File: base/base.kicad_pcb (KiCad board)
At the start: 2 copper layers, 100 x 100 mm, 20 parts, among them J1 FTDI, J2 Barrel_Jack, J3 CONN_01X40, SW1 SW_Push, U1 Z80CPU, U2 27C256, U3 7404, U4 55257, U5 7432, U6 16550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

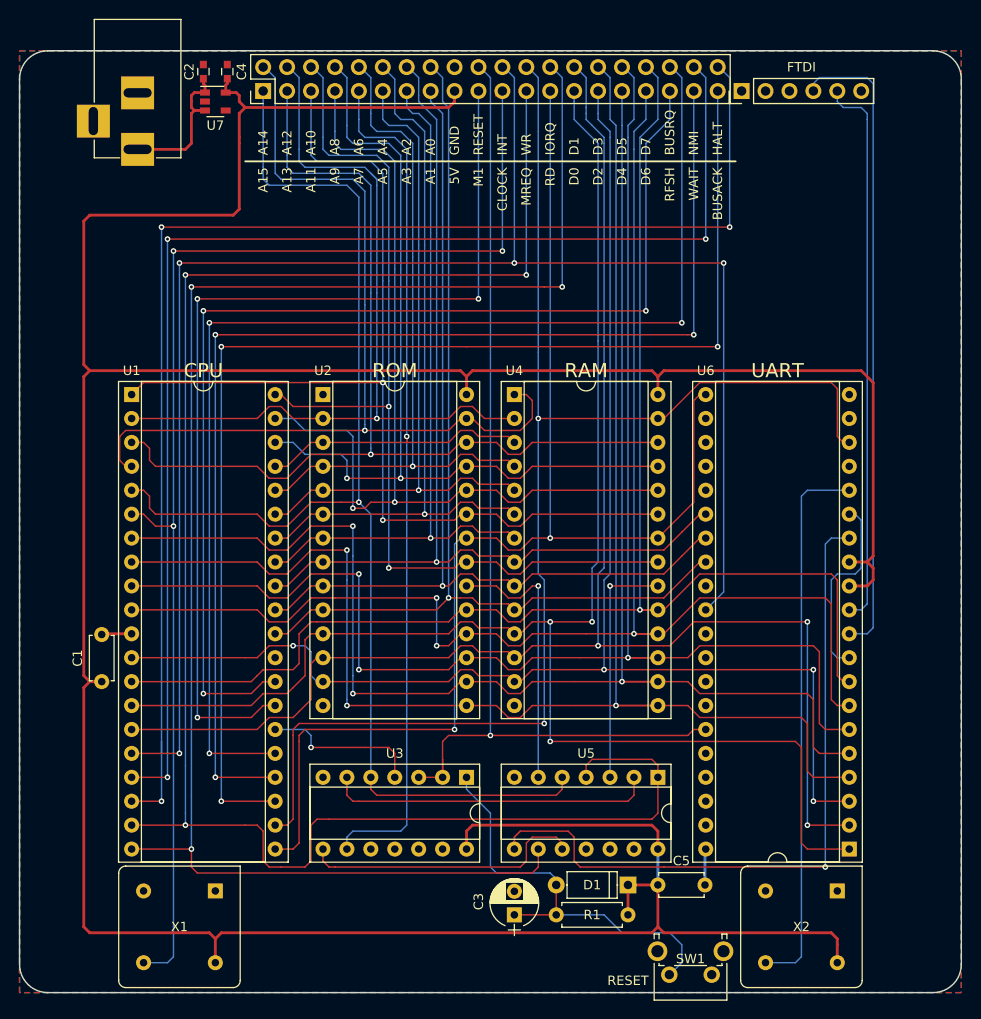
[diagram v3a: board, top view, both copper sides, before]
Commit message: Readded mounting holes
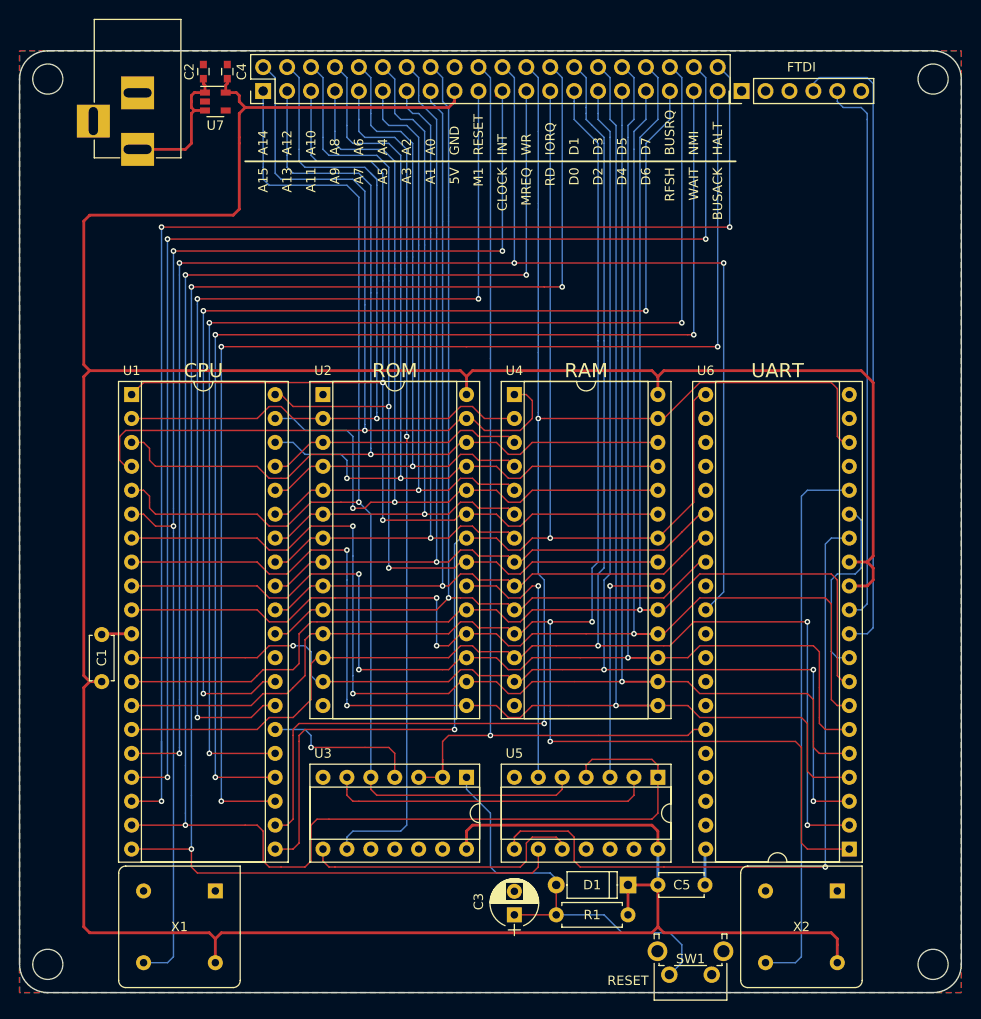
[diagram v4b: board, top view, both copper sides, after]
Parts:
- added REF**: MountingHole_3.2mm_M3, Mounting_Holes:MountingHole_3.2mm_M3, F.Cu at (151.1, 157.0)
- added REF**: MountingHole_3.2mm_M3, Mounting_Holes:MountingHole_3.2mm_M3, F.Cu at (57.1, 157.0)
- added REF**: MountingHole_3.2mm_M3, Mounting_Holes:MountingHole_3.2mm_M3, F.Cu at (57.1, 63.0)
- added REF**: MountingHole_3.2mm_M3, Mounting_Holes:MountingHole_3.2mm_M3, F.Cu at (151.1, 63.0)
- added REF***: OSHW-Symbol_6.7x6mm_SilkScreen, Symbols:OSHW-Symbol_6.7x6mm_SilkScreen, B.Cu at (104.1, 73.0)
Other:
- board text added: "6-20V"

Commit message: Redid power trace
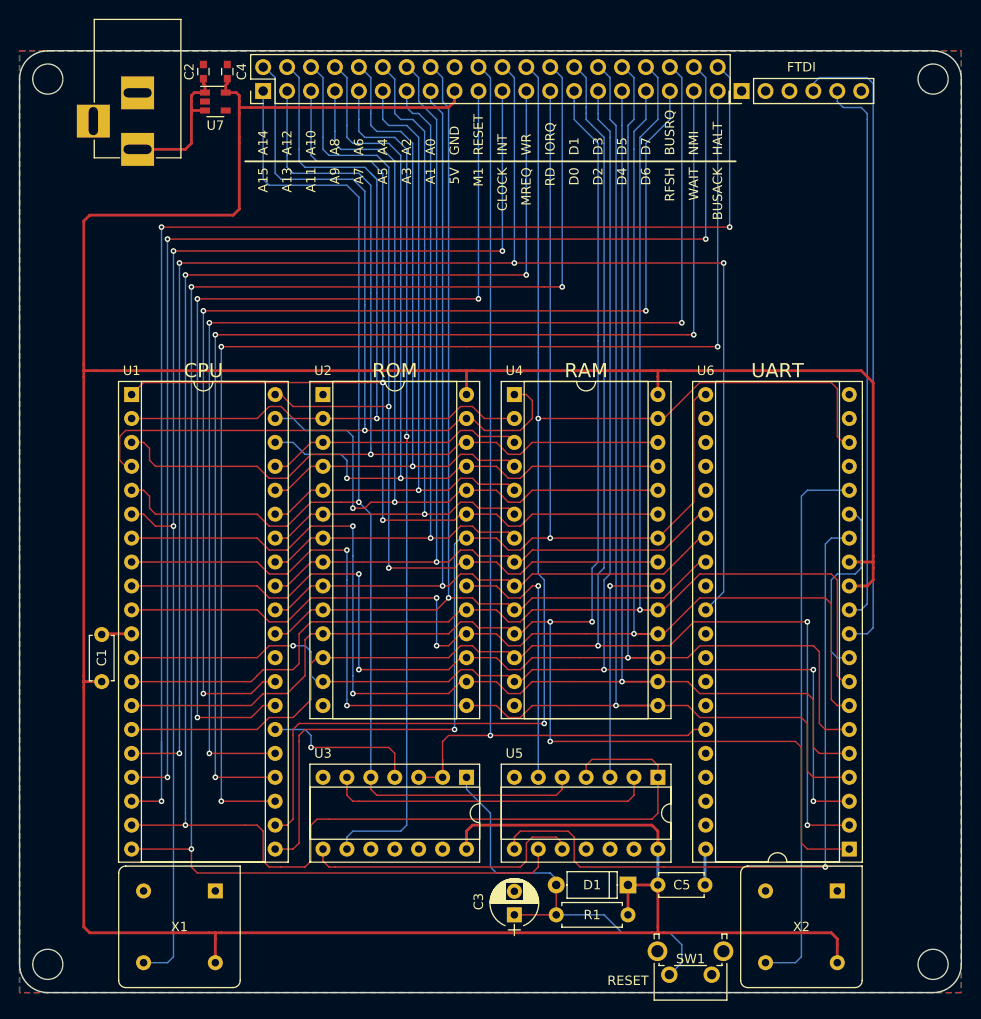
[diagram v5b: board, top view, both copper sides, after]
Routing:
- net +5V: track 374.9 -> 375.8 mm

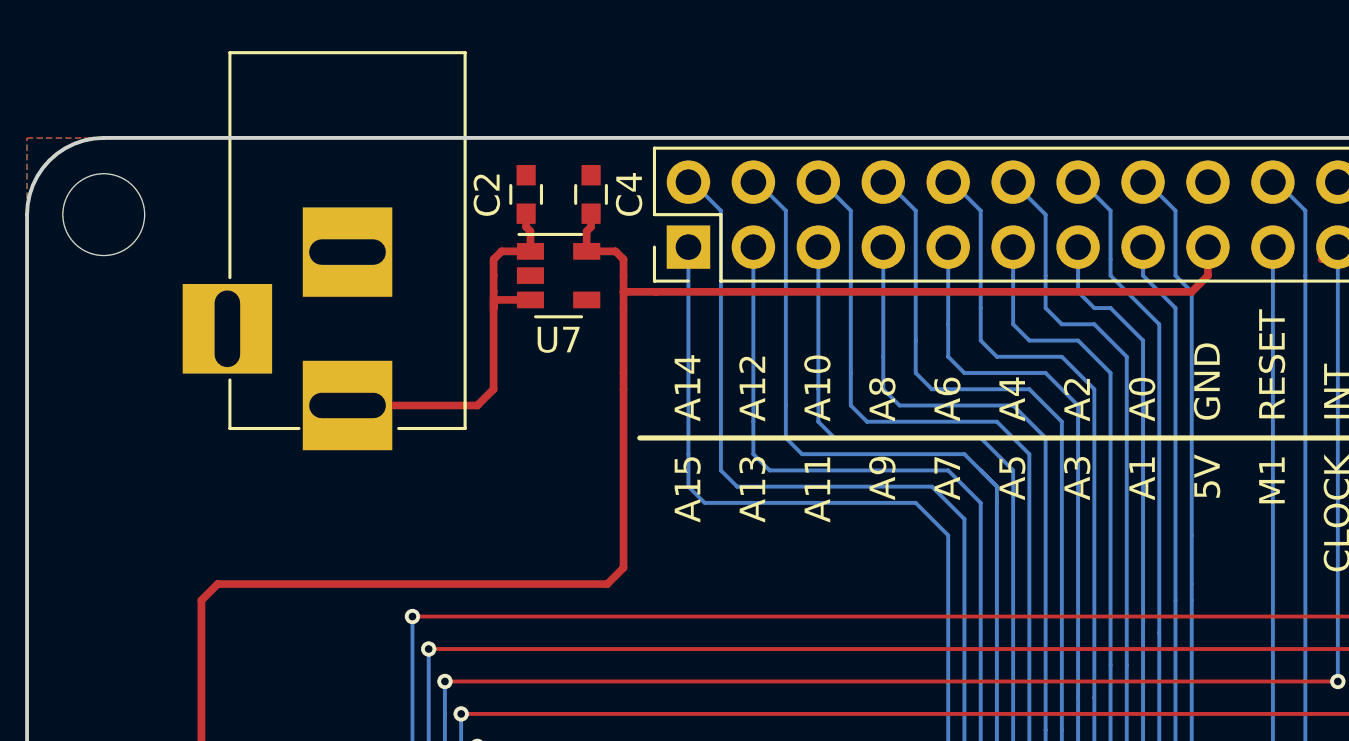
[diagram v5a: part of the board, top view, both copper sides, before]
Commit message: Increased size of voltage regulator
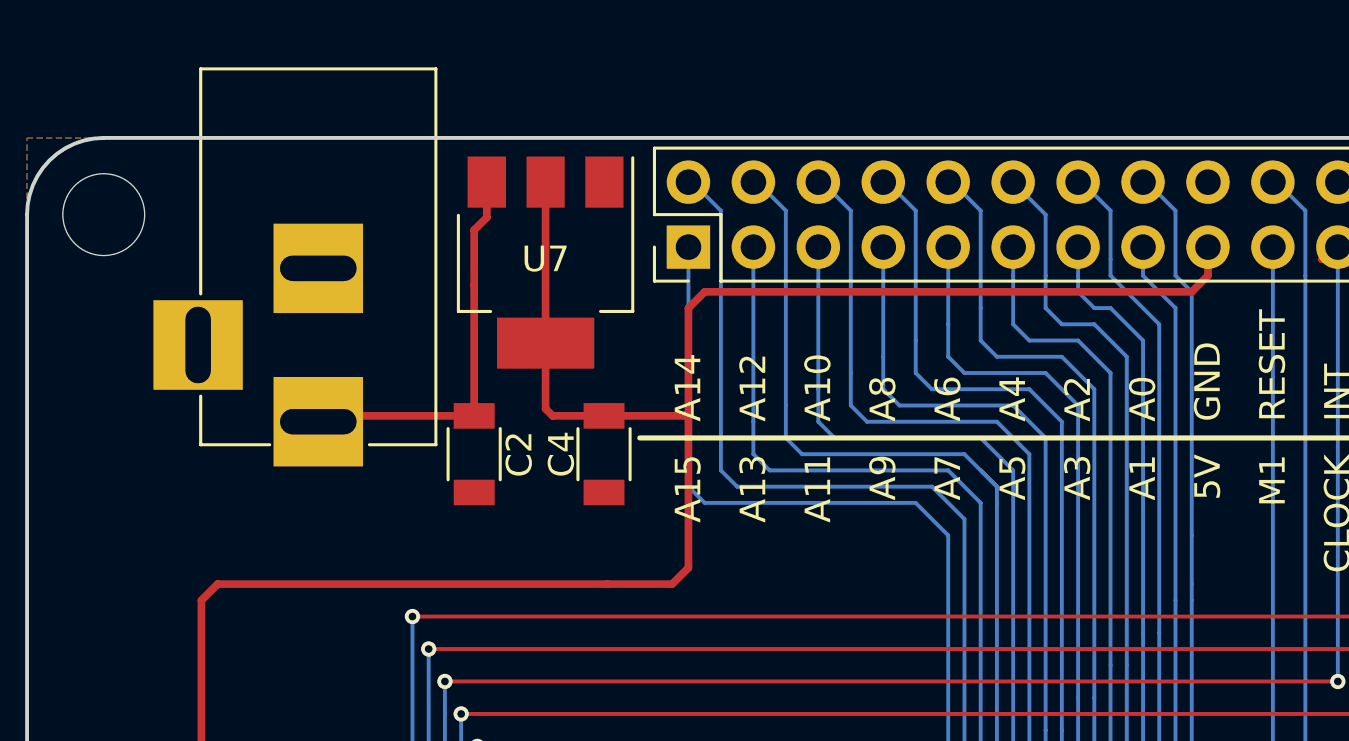
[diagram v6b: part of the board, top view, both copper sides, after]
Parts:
- C1: value .1 uF -> 1 uF
- C2, C4: value 1 uF -> 10 uF; footprint Capacitors_SMD:C_0603 -> Capacitors_SMD:C_1206
- C5: value .1 uF -> C_Small
- U7: value MIC5205-5.0 -> AP1117-50; footprint TO_SOT_Packages_SMD:SOT-23-5 -> TO_SOT_Packages_SMD:SOT-223-3Lead_TabPin2
- moved C2 10.4 mm to (71.6, 72.4), turned to 270 degrees
- moved C4 10.2 mm to (76.7, 72.4), turned to 270 degrees
- moved J2 1.31 mm to (65.5, 71.1)
- moved U7 0.72 mm to (74.4, 64.9), turned to 270 degrees
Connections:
- U7 pad 1: Net-(C2-Pad1) -> GND
- U7 pad 2: GND -> +5V
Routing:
- net +5V: track 375.8 -> 385.9 mm
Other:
- board text added: "7-15V"
- board text removed: "6-20V"

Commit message: Moved FTDI port
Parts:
- moved J1 2.54 mm to (133.3, 64.3)
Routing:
- net TX: track 68.3 -> 65.7 mm
- net RX: track 59.1 -> 56.9 mm
- net Net-(J1-Pad3): track 0.00 -> 0.79 mm
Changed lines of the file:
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@@
     (thickness 1.6)
     (drawings 57)
-    (tracks 1103)
+    (tracks 1102)
     (zones 0)
     (modules 25)
@@
   )
   (module Pin_Headers:Pin_Header_Straight_1x06_Pitch2.54mm (layer F.Cu)
-    (at 130.81 64.29 90)
+    (at 133.35 64.29 90)
     (descr "Through hole straight pin header, 1x06, 2.54mm pitch, single row")
     (tags "Through hole pin header THT 1x06 2.54mm single row")
@@
   (segment (start 104.14 92.71) (end 104.14 132.715) (width 0.152) (layer B.Cu) (net 55))
   (via (at 104.14 132.715) (size 0.6) (drill 0.3) (layers F.Cu B.Cu) (net 55))
+  (segment (start 144.145 66.675) (end 143.51 66.04) (width 0.152) (layer B.Cu) (net 58))
+  (segment (start 143.51 66.04) (end 143.51 64.29) (width 0.152) (layer B.Cu) (net 58) (status 800000))
   (segment (start 144.145 67.31) (end 144.145 118.745) (width 0.152) (layer B.Cu) (net 58))
-  (segment (start 140.97 65.405) (end 141.605 66.04) (width 0.152) (layer B.Cu) (net 58))
-  (segment (start 141.605 66.04) (end 143.51 66.04) (width 0.152) (layer B.Cu) (net 58))
-  (segment (start 143.51 66.04) (end 144.145 66.675) (width 0.152) (layer B.Cu) (net 58))
   (segment (start 144.145 66.675) (end 144.145 67.31) (width 0.152) (layer B.Cu) (net 58))
-  (segment (start 140.97 64.29) (end 140.97 65.405) (width 0.152) (layer B.Cu) (net 58) (status 400010))
   (segment (start 143.51 119.38) (end 142.24 119.38) (width 0.152) (layer B.Cu) (net 58) (status 800020))
   (segment (start 144.145 118.745) (end 143.51 119.38) (width 0.152) (layer B.Cu) (net 58))
+  (segment (start 141.605 62.865) (end 140.97 63.5) (width 0.152) (layer B.Cu) (net 59) (status 800000))
+  (segment (start 140.97 63.5) (end 140.97 64.29) (width 0.152) (layer B.Cu) (net 59) (status C00000))
   (segment (start 142.24 121.92) (end 144.145 121.92) (width 0.152) (layer B.Cu) (net 59) (status 400010))
-  (segment (start 139.065 62.865) (end 138.43 63.5) (width 0.152) (layer B.Cu) (net 59) (status 800020))
-  (segment (start 144.145 62.865) (end 139.065 62.865) (width 0.152) (layer B.Cu) (net 59))
+  (segment (start 144.145 62.865) (end 141.605 62.865) (width 0.152) (layer B.Cu) (net 59))
   (segment (start 144.78 63.5) (end 144.145 62.865) (width 0.152) (layer B.Cu) (net 59))
   (segment (start 144.78 121.285) (end 144.78 63.5) (width 0.152) (layer B.Cu) (net 59))
   (segment (start 144.145 121.92) (end 144.78 121.285) (width 0.152) (layer B.Cu) (net 59))
-  (segment (start 138.43 63.5) (end 138.43 64.29) (width 0.152) (layer B.Cu) (net 59) (status C00030))
+  (segment (start 138.43 63.5) (end 138.43 64.29) (width 0.152) (layer B.Cu) (net 71) (status C00030))
   (segment (start 80.645 110.49) (end 79.375 109.22) (width 0.152) (layer F.Cu) (net 61))
   (segment (start 67.945 108.585) (end 67.945 107.95) (width 0.152) (layer F.Cu) (net 61))
